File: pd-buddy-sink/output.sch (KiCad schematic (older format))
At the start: 7 parts, among them J1 5-20 V⎓, Q1 MMBT3904, Q2 DMP4015SSS

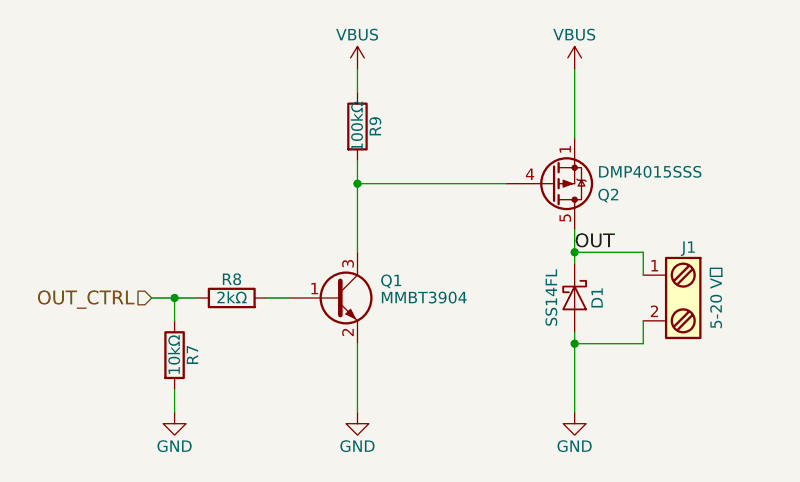
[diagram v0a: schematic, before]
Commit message: Changed Q2 and D1
D1 is now a B140, which is a MacroFab house part.  It's actually a bit
more expensive from distributors than the SS14FL, but the lack of a
labor charge makes it quite a bit cheaper for PCBA.  It's also larger,
so in order to fit the new part, I moved it between Q2 and J1.  This is
possible because…

Q2 is now a DMP3017SFG.  This is a cheaper, smaller, and less
over-specified MOSFET which should be fine for the job of controlling
the PD Buddy Sink's output.  It uses a proprietary Diodes Inc. package
whose footprint I contributed to KiCad's library.  Because the new
MOSFET is so much smaller than the old one, I was able to fit it close
to the board edge where R9 used to be.

The whole output circuit has been rearranged, and I like its layout a
lot more now.  Also, the new position of D1 allowed me to move a bunch
of reference designators closer to their footprints, which is nice.
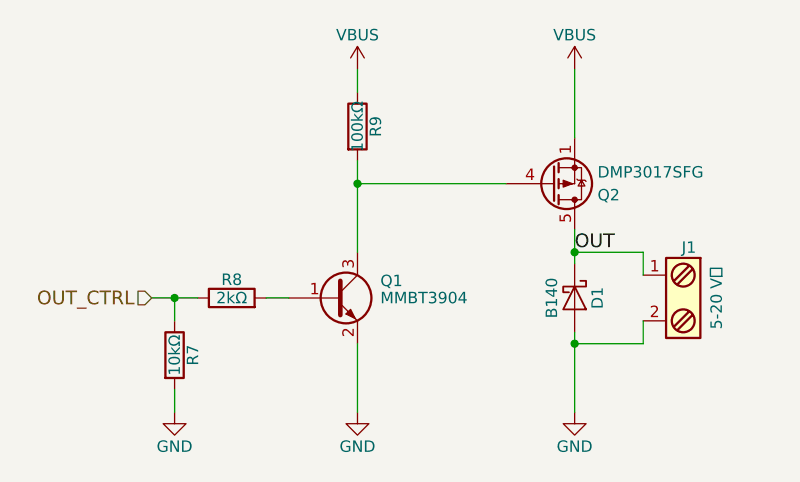
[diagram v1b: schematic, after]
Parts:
- removed Q2: DMP4015SSS, Housings_SOIC:SOIC-8_3.9x4.9mm_Pitch1.27mm, symbol DMP4015SSS
- added Q2: DMP3017SFG, Housings_SON:Diodes_PowerDI3333-8, symbol DMP3017SFG
- D1: value SS14FL -> B140; footprint Diodes_SMD:D_SOD-123F -> Diodes_SMD:D_SMA
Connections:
- net OUT: now also Q2.5 (D)
- net VBUS: now also Q2.1 (S), Q2.2 (S), Q2.3 (S)
- net at Q1.3 (C), R9.2: now also Q2.4 (G)
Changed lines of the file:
@@
 $EndDescr
-$Comp
-L DMP4015SSS Q2
-U 1 1 588FA570
-P 6400 3550
-F 0 "Q2" H 6600 3600 50  0000 L CNN
-F 1 "DMP4015SSS" H 6600 3500 50  0000 L CNN
-F 2 "Housings_SOIC:SOIC-8_3.9x4.9mm_Pitch1.27mm" H 6600 3650 50  0001 C CNN
-F 3 "http://www.diodes.com/_files/datasheets/DMP4015SSS.pdf" H 6600 3600 50  0001 C CNN
-	1    6400 3550
-	1    0    0    1
-$EndComp
 $Comp
 L Screw_Terminal_1x02 J1
@@
 P 6500 4050
 F 0 "D1" H 6500 4150 50  0000 C CNN
-F 1 "SS14FL" H 6500 3950 50  0000 C CNN
-F 2 "Diodes_SMD:D_SOD-123F" H 6500 4050 50  0001 C CNN
-F 3 "https://www.fairchildsemi.com/datasheets/SS/SS14FL.pdf" H 6500 4050 50  0001 C CNN
+F 1 "B140" H 6500 3950 50  0000 C CNN
+F 2 "Diodes_SMD:D_SMA" H 6500 4050 50  0001 C CNN
+F 3 "https://www.diodes.com/assets/Datasheets/ds13002.pdf" H 6500 4050 50  0001 C CNN
 	1    6500 4050
 	0    1    1    0
@@
 	1    0    0    -1
 $EndComp
+$Comp
+L DMP3017SFG Q2
+U 1 1 596D6EFB
+P 6400 3550
+F 0 "Q2" H 6600 3600 50  0000 L CNN
+F 1 "DMP3017SFG" H 6600 3500 50  0000 L CNN
+F 2 "Housings_SON:Diodes_PowerDI3333-8" H 6600 3650 50  0001 C CNN
+F 3 "https://www.diodes.com/assets/Datasheets/DMP3017SFG.pdf" H 6600 3600 50  0001 C CNN
+	1    6400 3550
+	1    0    0    1
+$EndComp
 $EndSCHEMATC

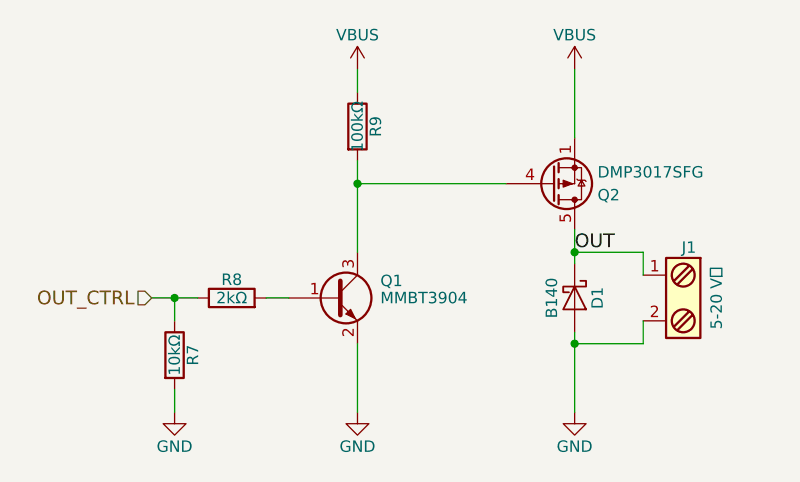
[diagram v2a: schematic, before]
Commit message: Added test points, replaced SW1 with R11
More test points will be needed for automated testing, so I've added the
first two I know of.

With firmware version 1.2.0+, there's not much reason to install SW1
anymore.  This commit replaces it with R11, an unpopulated resistor
footprint that does the same thing as bridging the two pins of SW1 used
to do, just in case an upgrade make the `boot` command stop working.
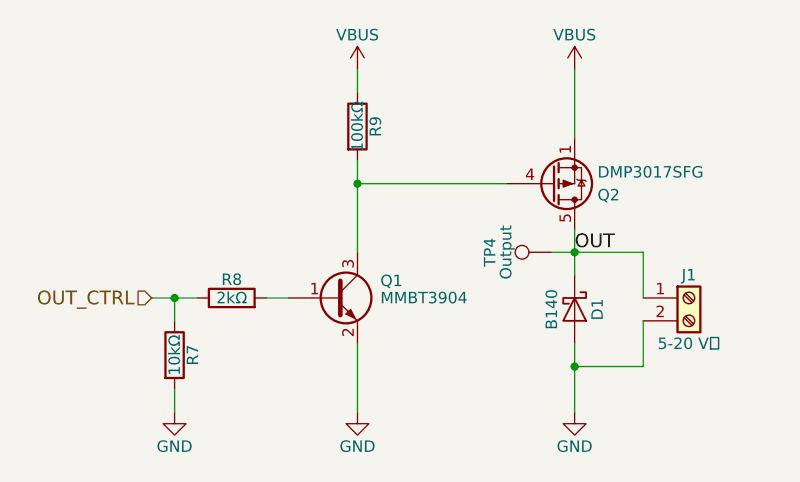
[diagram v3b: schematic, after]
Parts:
- removed J1: 5-20 V⎓, Connectors_Terminal_Blocks:TerminalBlock_Pheonix_MPT-2.54mm_2pol, symbol Screw_Terminal_1x02
- added J1: 5-20 V⎓, Connectors_Terminal_Blocks:TerminalBlock_Pheonix_MPT-2.54mm_2pol, symbol Screw_Terminal_01x02
- added TP4: Output, Measurement_Points:Measurement_Point_Round-SMD-Pad_Small, symbol Test_Point
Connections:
- net GND: now also J1.2 (Pin_2)
- net OUT: now also J1.1 (Pin_1), TP4.1
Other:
- moved on the sheet: D1
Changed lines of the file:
@@
 Comment4 ""
 $EndDescr
-$Comp
-L Screw_Terminal_1x02 J1
-U 1 1 588FA688
-P 7000 4050
-F 0 "J1" H 7000 4300 50  0000 C TNN
-F 1 "5-20 V⎓" V 6850 4050 50  0000 C TNN
-F 2 "Connectors_Terminal_Blocks:TerminalBlock_Pheonix_MPT-2.54mm_2pol" H 7000 3825 50  0001 C CNN
-F 3 "" H 6975 4050 50  0001 C CNN
-	1    7000 4050
-	-1   0    0    -1
-$EndComp
 Text HLabel 4650 4050 0    60   Input ~ 0
 OUT_CTRL
@@
 	5150 4050 5250 4050
 $Comp
-L GND #PWR023
+L GND #PWR022
 U 1 1 58925B13
 P 5550 4550
-F 0 "#PWR023" H 5550 4300 50  0001 C CNN
+F 0 "#PWR022" H 5550 4300 50  0001 C CNN
 F 1 "GND" H 5550 4400 50  0000 C CNN
 F 2 "" H 5550 4550 50  0000 C CNN
@@
 	5550 4550 5550 4250
 $Comp
-L GND #PWR024
+L GND #PWR023
 U 1 1 58925CFD
 P 6500 4550
-F 0 "#PWR024" H 6500 4300 50  0001 C CNN
+F 0 "#PWR023" H 6500 4300 50  0001 C CNN
 F 1 "GND" H 6500 4400 50  0000 C CNN
 F 2 "" H 6500 4550 50  0000 C CNN
@@
 L D_Schottky D1
 U 1 1 58925D4E
-P 6500 4050
-F 0 "D1" H 6500 4150 50  0000 C CNN
-F 1 "B140" H 6500 3950 50  0000 C CNN
-F 2 "Diodes_SMD:D_SMA" H 6500 4050 50  0001 C CNN
-F 3 "https://www.diodes.com/assets/Datasheets/ds13002.pdf" H 6500 4050 50  0001 C CNN
-	1    6500 4050
+P 6500 4100
+F 0 "D1" H 6500 4200 50  0000 C CNN
+F 1 "B140" H 6500 4000 50  0000 C CNN
+F 2 "Diodes_SMD:D_SMA" H 6500 4100 50  0001 C CNN
+F 3 "https://www.diodes.com/assets/Datasheets/ds13002.pdf" H 6500 4100 50  0001 C CNN
+	1    6500 4100
 	0    1    1    0
 $EndComp
 Wire Wire Line
-	6500 3750 6500 3900
+	6500 3750 6500 3950
 Wire Wire Line
-	6500 4200 6500 4550
+	6500 4250 6500 4550
 Wire Wire Line
-	6500 3850 6800 3850
+	6400 3850 6800 3850
 Wire Wire Line
-	6800 3850 6800 3950
+	6800 3850 6800 4050
 Connection ~ 6500 3850
 Wire Wire Line
-	6800 4150 6800 4250
+	6800 4150 6800 4350
 Wire Wire Line
-	6800 4250 6500 4250
-Connection ~ 6500 4250
+	6800 4350 6500 4350
+Connection ~ 6500 4350
 Wire Wire Line
 	5550 3450 5550 3850
@@
 Connection ~ 4750 4050
 $Comp
-L GND #PWR025
+L GND #PWR024
 U 1 1 58926FD3
 P 4750 4550
-F 0 "#PWR025" H 4750 4300 50  0001 C CNN
+F 0 "#PWR024" H 4750 4300 50  0001 C CNN
 F 1 "GND" H 4750 4400 50  0000 C CNN
 F 2 "" H 4750 4550 50  0000 C CNN
@@
 OUT
 $Comp
-L VBUS #PWR026
+L VBUS #PWR025
 U 1 1 592B5EAB
 P 5550 3050
-F 0 "#PWR026" H 5550 2900 50  0001 C CNN
+F 0 "#PWR025" H 5550 2900 50  0001 C CNN
 F 1 "VBUS" H 5550 3200 50  0000 C CNN
 F 2 "" H 5550 3050 50  0001 C CNN
@@
 $EndComp
 $Comp
-L VBUS #PWR027
+L VBUS #PWR026
 U 1 1 592B5EB8
 P 6500 3050
-F 0 "#PWR027" H 6500 2900 50  0001 C CNN
+F 0 "#PWR026" H 6500 2900 50  0001 C CNN
 F 1 "VBUS" H 6500 3200 50  0000 C CNN
 F 2 "" H 6500 3050 50  0001 C CNN
@@
 	1    0    0    1
 $EndComp
+$Comp
+L Test_Point TP4
+U 1 1 5A937B77
+P 6400 3850
+F 0 "TP4" H 6400 4120 50  0000 C CNN
+F 1 "Output" H 6400 4050 50  0000 C CNN
+F 2 "Measurement_Points:Measurement_Point_Round-SMD-Pad_Small" H 6600 3850 50  0001 C CNN
+F 3 "" H 6600 3850 50  0001 C CNN
+	1    6400 3850
+	0    -1   -1   0
+$EndComp
+$Comp
+L Screw_Terminal_01x02 J1
+U 1 1 5A938FC2
+P 7000 4050
+F 0 "J1" H 7000 4150 50  0000 C CNN
+F 1 "5-20 V⎓" H 7000 3850 50  0000 C CNN
+F 2 "Connectors_Terminal_Blocks:TerminalBlock_Pheonix_MPT-2.54mm_2pol" H 7000 4050 50  0001 C CNN
+F 3 "" H 7000 4050 50  0001 C CNN
+	1    7000 4050
+	1    0    0    -1
+$EndComp
 $EndSCHEMATC

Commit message: Update to KiCad 5.0 nightly
Hooray, new stuff!  The STM32 symbol is a reasonable size now!  We have
a sym-lib-table!  Everything is great, and I'm excited!

The board's a bit of a mess though, as the silkscreen needs to be laid
out nicely.  Oh well, details.
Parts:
- removed D1: B140, Diodes_SMD:D_SMA, symbol D_Schottky
- removed Q1: MMBT3904, TO_SOT_Packages_SMD:SOT-23, symbol MMBT3904
- removed R7: 10kΩ, Resistors_SMD:R_0402, symbol R
- removed R8: 2kΩ, Resistors_SMD:R_0402, symbol R
- removed R9: 100kΩ, Resistors_SMD:R_0402, symbol R
- removed TP4: Output, Measurement_Points:Measurement_Point_Round-SMD-Pad_Small, symbol Test_Point
- added D1: B140-E3, Diode_SMD:D_SMA, symbol Diode:B140-E3
- added Q1: MMBT3904, Package_TO_SOT_SMD:SOT-23, symbol Transistor_BJT:MMBT3904
- added R7: 10kΩ, Resistor_SMD:R_0402_1005Metric, symbol Device:R
- added R8: 2kΩ, Resistor_SMD:R_0402_1005Metric, symbol Device:R
- added R9: 100kΩ, Resistor_SMD:R_0402_1005Metric, symbol Device:R
- added TP4: Output, TestPoint:TestPoint_Pad_D1.5mm, symbol Connector:Test_Point
- J1: footprint Connectors_Terminal_Blocks:TerminalBlock_Pheonix_MPT-2.54mm_2pol -> TerminalBlock_Phoenix:TerminalBlock_Phoenix_MPT-0,5-2-2.54_1x02_P2.54mm_Horizontal; symbol Screw_Terminal_01x02 -> Connector:Screw_Terminal_01x02
- Q2: footprint Housings_SON:Diodes_PowerDI3333-8 -> Package_SON:Diodes_PowerDI3333-8; symbol DMP3017SFG -> pd-buddy:DMP3017SFG
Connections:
- net GND: now also D1.2 (A), Q1.2 (E), R7.2
- net OUT: now also D1.1 (K), TP4.1
- net OUT_CTRL: now also R7.1, R8.1
- net VBUS: now also R9.1
- net at Q2.4 (G): now also Q1.3 (C), R9.2
- new net: Q1.1 (B), R8.2
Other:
- moved on the sheet: J1
